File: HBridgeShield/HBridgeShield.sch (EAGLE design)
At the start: 5 parts, among them X1 22-23-2041

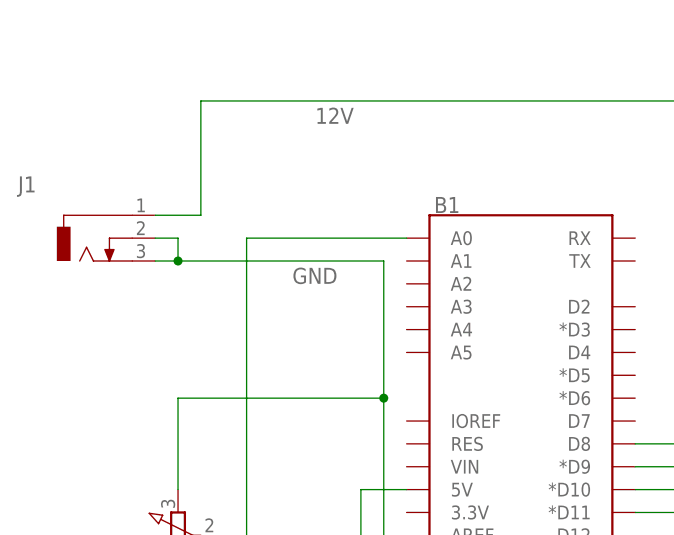
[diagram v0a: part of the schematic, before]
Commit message: No deadly power connection
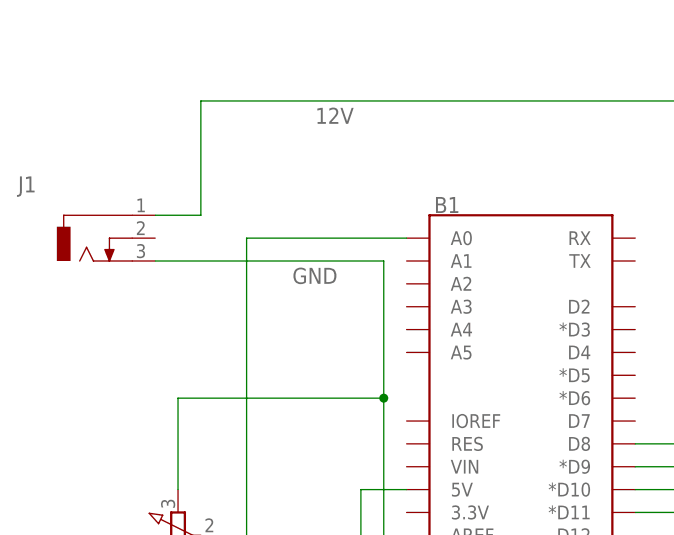
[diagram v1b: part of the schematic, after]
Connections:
- net GND: no longer J1.2
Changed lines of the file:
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@@
 <net name="GND" class="0">
 <segment>
-<pinref part="J1" gate="G$1" pin="2"/>
 <pinref part="J1" gate="G$1" pin="3"/>
-<wire x1="5.08" y1="60.96" x2="7.62" y2="60.96" width="0.1524" layer="91"/>
 <pinref part="ZX1" gate="G$1" pin="4"/>
-<wire x1="7.62" y1="60.96" x2="30.48" y2="60.96" width="0.1524" layer="91"/>
+<wire x1="5.08" y1="60.96" x2="30.48" y2="60.96" width="0.1524" layer="91"/>
 <wire x1="91.44" y1="48.26" x2="86.36" y2="48.26" width="0.1524" layer="91"/>
 <wire x1="86.36" y1="48.26" x2="86.36" y2="45.72" width="0.1524" layer="91"/>
@@
 <wire x1="7.62" y1="45.72" x2="30.48" y2="45.72" width="0.1524" layer="91"/>
 <junction x="30.48" y="45.72"/>
-<wire x1="5.08" y1="63.5" x2="7.62" y2="63.5" width="0.1524" layer="91"/>
-<wire x1="7.62" y1="63.5" x2="7.62" y2="60.96" width="0.1524" layer="91"/>
-<junction x="7.62" y="60.96"/>
 </segment>
 </net>

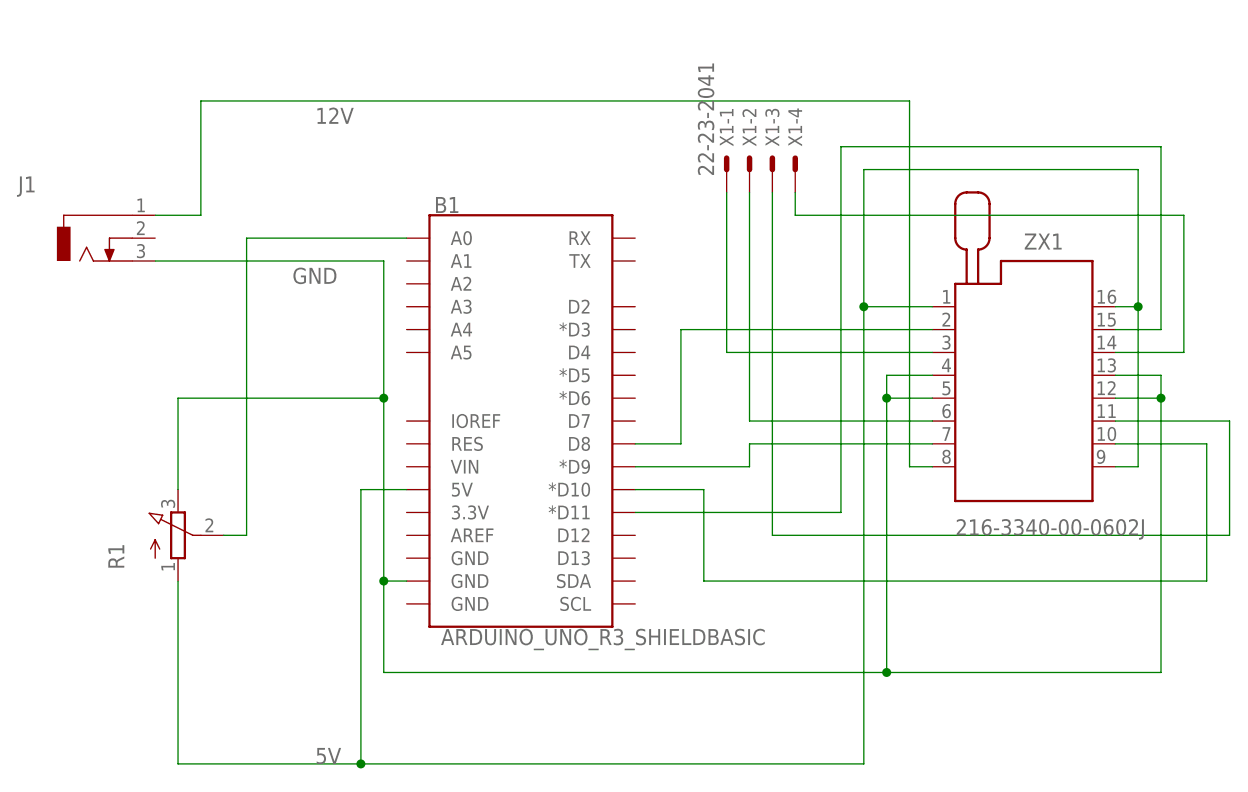
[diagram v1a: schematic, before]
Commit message: Added 12v connection to Arduino board VIN
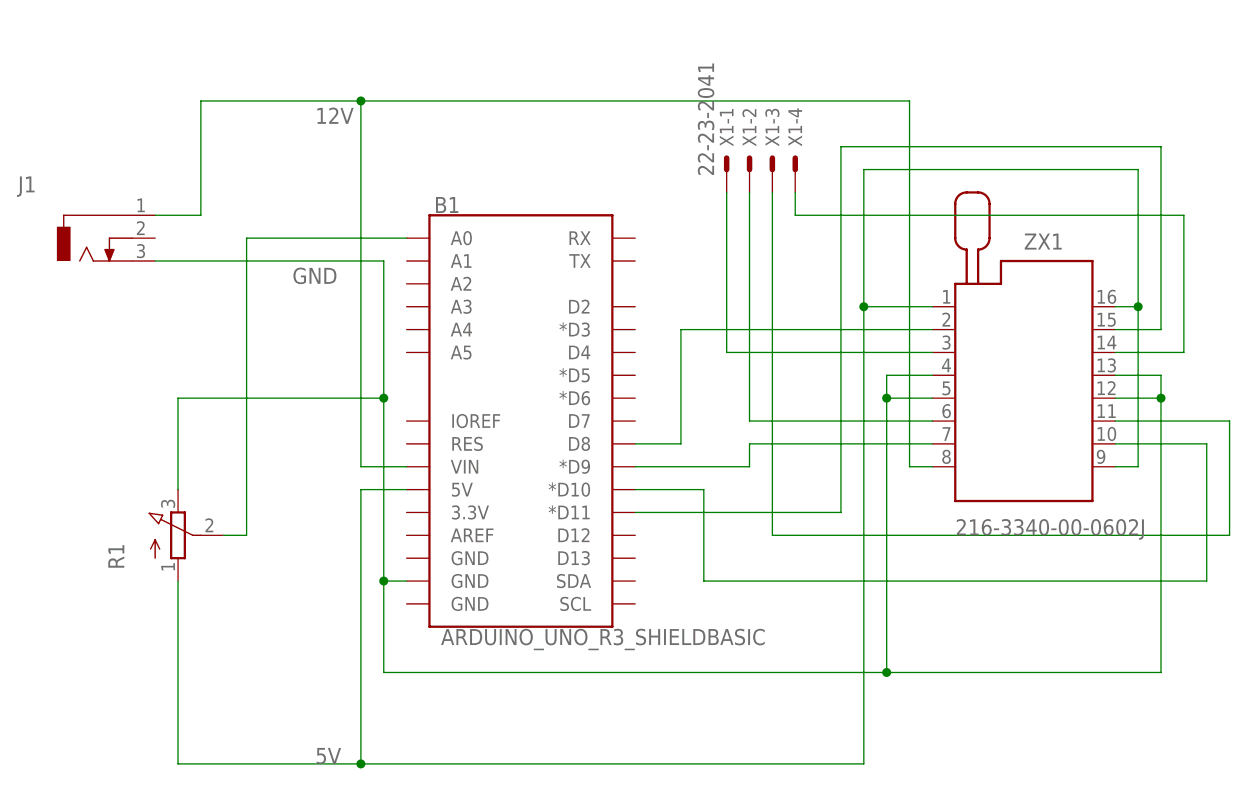
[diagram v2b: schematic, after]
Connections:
- net 12V: now also B1.VIN
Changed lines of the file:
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@@
 <wire x1="91.44" y1="38.1" x2="88.9" y2="38.1" width="0.1524" layer="91"/>
 <wire x1="88.9" y1="38.1" x2="88.9" y2="78.74" width="0.1524" layer="91"/>
-<wire x1="88.9" y1="78.74" x2="10.16" y2="78.74" width="0.1524" layer="91"/>
+<wire x1="88.9" y1="78.74" x2="27.94" y2="78.74" width="0.1524" layer="91"/>
 <pinref part="J1" gate="G$1" pin="1"/>
+<wire x1="27.94" y1="78.74" x2="10.16" y2="78.74" width="0.1524" layer="91"/>
 <wire x1="10.16" y1="78.74" x2="10.16" y2="66.04" width="0.1524" layer="91"/>
 <wire x1="10.16" y1="66.04" x2="5.08" y2="66.04" width="0.1524" layer="91"/>
 <label x="22.86" y="76.2" size="1.778" layer="95"/>
+<wire x1="27.94" y1="78.74" x2="27.94" y2="38.1" width="0.1524" layer="91"/>
+<junction x="27.94" y="78.74"/>
+<pinref part="B1" gate="G$1" pin="VIN"/>
+<wire x1="27.94" y1="38.1" x2="33.02" y2="38.1" width="0.1524" layer="91"/>
 </segment>
 </net>
